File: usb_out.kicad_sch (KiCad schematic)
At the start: 30 parts, among them J6 USB_C_Receptacle_USB2.0, Q22 2N7002, U12 SY8105, U13 LM75B, U14 INA219AxD

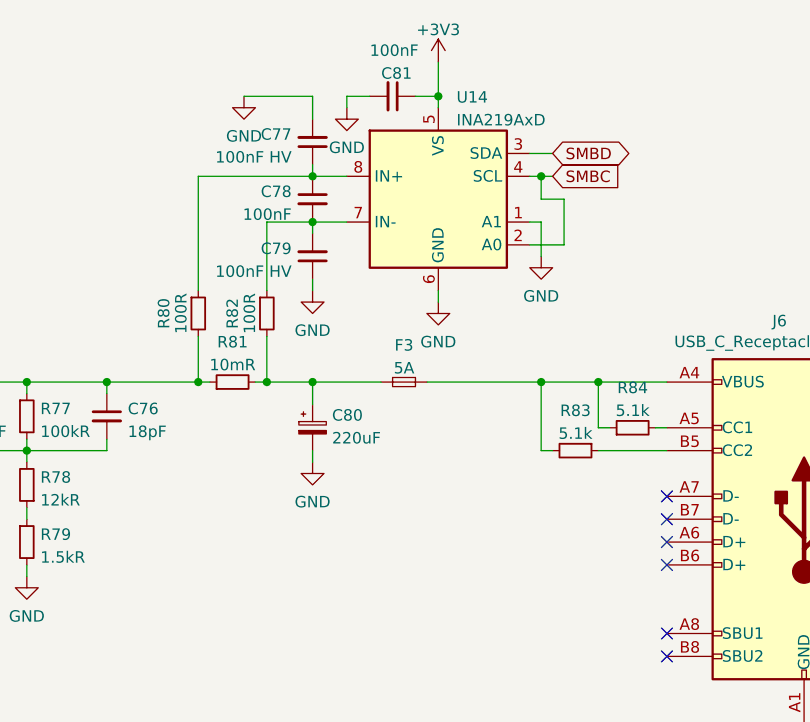
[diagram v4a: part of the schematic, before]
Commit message: Charger and step-down component placement
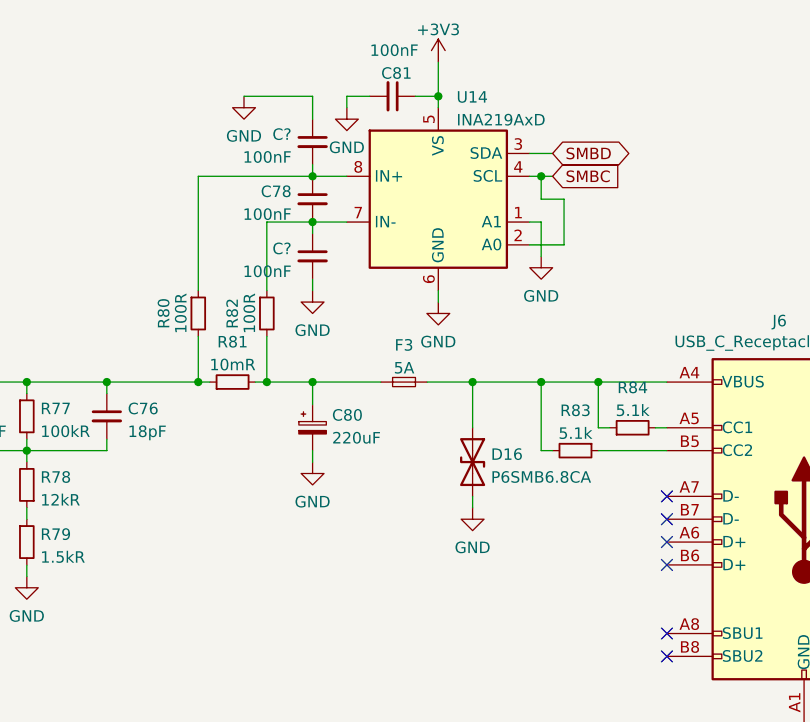
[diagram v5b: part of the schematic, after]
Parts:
- removed C77, C79: 100nF HV, Capacitor_SMD:C_0603_1608Metric, symbol Device:C_Small
- added C? (x2): 100nF, Capacitor_SMD:C_0402_1005Metric, symbol Device:C_Small
- added D16: P6SMB6.8CA, Diode_SMD:D_SMB, symbol Device:D_TVS
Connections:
- net GND: now also C?.1, C?.2, D16.2 (A2)
- net at F3.2, J6.A4 (VBUS), J6.A9 (VBUS)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: now also D16.1 (A1)
- net at C78.2, R82.1, U14.7 (IN-): now also C?.1
- net at C78.1, R80.1, U14.8 (IN+): now also C?.2
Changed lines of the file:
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@@
   (junction (at 142.24 66.04) (diameter 0) (color 0 0 0 0)
+  )
+  (junction (at 165.1 66.04) (diameter 0) (color 0 0 0 0)
   )
   (junction (at 179.07 66.04) (diameter 0) (color 0 0 0 0)
@@
     (stroke (width 0) (type default) (color 0 0 0 0))
   )
+  (wire (pts (xy 165.1 66.04) (xy 165.1 71.12))
+    (stroke (width 0) (type default) (color 0 0 0 0))
+  )
   (wire (pts (xy 81.28 129.54) (xy 82.55 129.54))
     (stroke (width 0) (type default) (color 0 0 0 0))
@@
     (stroke (width 0) (type default) (color 0 0 0 0))
   )
-  (wire (pts (xy 160.02 66.04) (xy 172.72 66.04))
+  (wire (pts (xy 160.02 66.04) (xy 165.1 66.04))
     (stroke (width 0) (type default) (color 0 0 0 0))
   )
@@
     (stroke (width 0) (type default) (color 0 0 0 0))
   )
+  (wire (pts (xy 165.1 78.74) (xy 165.1 80.01))
+    (stroke (width 0) (type default) (color 0 0 0 0))
+  )
   (wire (pts (xy 82.55 115.57) (xy 82.55 116.84))
     (stroke (width 0) (type default) (color 0 0 0 0))
@@
   )
   (wire (pts (xy 105.41 125.73) (xy 105.41 129.54))
+    (stroke (width 0) (type default) (color 0 0 0 0))
+  )
+  (wire (pts (xy 165.1 66.04) (xy 172.72 66.04))
     (stroke (width 0) (type default) (color 0 0 0 0))
   )
@@
     (pin "1")
   )
-  (symbol (lib_id "Device:C_Small") (at 147.32 52.07 0) (mirror x) (unit 1)
-    (in_bom yes) (on_board yes) (fields_autoplaced)
-    (property "Reference" "C79" (id 0) (at 144.996 51.2289 0)
-      (effects (font (size 1.27 1.27)) (justify right))
-    )
-    (property "Value" "100nF HV" (id 1) (at 144.996 53.7658 0)
-      (effects (font (size 1.27 1.27)) (justify right))
-    )
-    (property "Footprint" "Capacitor_SMD:C_0603_1608Metric" (id 2) (at 147.32 52.07 0)
-      (effects (font (size 1.27 1.27)) hide)
-    )
-    (property "Datasheet" "~" (id 3) (at 147.32 52.07 0)
-      (effects (font (size 1.27 1.27)) hide)
-    )
-    (property "LCSC" "C14663" (id 4) (at 147.32 52.07 90)
-      (effects (font (size 1.27 1.27)) hide)
-    )
-    (pin "1")
-    (pin "2")
-  )
   (symbol (lib_id "Regulator_Switching_Silergy:SY8105") (at 78.74 68.58 0) (unit 1)
     (in_bom yes) (on_board yes) (fields_autoplaced)
@@
     )
     (pin "1")
+  )
+  (symbol (lib_id "Device:D_TVS") (at 165.1 74.93 270) (unit 1)
+    (in_bom yes) (on_board yes) (fields_autoplaced)
+    (property "Reference" "D16" (id 0) (at 167.132 74.0953 90)
+      (effects (font (size 1.27 1.27)) (justify left))
+    )
+    (property "Value" "P6SMB6.8CA" (id 1) (at 167.132 76.6322 90)
+      (effects (font (size 1.27 1.27)) (justify left))
+    )
+    (property "Footprint" "Diode_SMD:D_SMB" (id 2) (at 165.1 74.93 0)
+      (effects (font (size 1.27 1.27)) hide)
+    )
+    (property "Datasheet" "~" (id 3) (at 165.1 74.93 0)
+      (effects (font (size 1.27 1.27)) hide)
+    )
+    (property "LCSC" "C78395" (id 4) (at 165.1 74.93 90)
+      (effects (font (size 1.27 1.27)) hide)
+    )
+    (pin "1")
+    (pin "2")
   )
   (symbol (lib_id "power:GND") (at 92.71 143.51 0) (unit 1)
@@
     )
     (pin "1")
-  )
-  (symbol (lib_id "Device:C_Small") (at 147.32 39.37 0) (mirror x) (unit 1)
-    (in_bom yes) (on_board yes) (fields_autoplaced)
-    (property "Reference" "C77" (id 0) (at 144.996 38.5289 0)
-      (effects (font (size 1.27 1.27)) (justify right))
-    )
-    (property "Value" "100nF HV" (id 1) (at 144.996 41.0658 0)
-      (effects (font (size 1.27 1.27)) (justify right))
-    )
-    (property "Footprint" "Capacitor_SMD:C_0603_1608Metric" (id 2) (at 147.32 39.37 0)
-      (effects (font (size 1.27 1.27)) hide)
-    )
-    (property "Datasheet" "~" (id 3) (at 147.32 39.37 0)
-      (effects (font (size 1.27 1.27)) hide)
-    )
-    (property "LCSC" "C14663" (id 4) (at 147.32 39.37 90)
-      (effects (font (size 1.27 1.27)) hide)
-    )
-    (pin "1")
-    (pin "2")
   )
   (symbol (lib_id "power:GND") (at 139.7 34.29 0) (unit 1)
@@
     (pin "8")
   )
+  (symbol (lib_id "Device:C_Small") (at 147.32 39.37 0) (mirror y) (unit 1)
+    (in_bom yes) (on_board yes)
+    (property "Reference" "C?" (id 0) (at 144.9959 38.5416 0)
+      (effects (font (size 1.27 1.27)) (justify left))
+    )
+    (property "Value" "100nF" (id 1) (at 144.9959 41.0785 0)
+      (effects (font (size 1.27 1.27)) (justify left))
+    )
+    (property "Footprint" "Capacitor_SMD:C_0402_1005Metric" (id 2) (at 147.32 39.37 0)
+      (effects (font (size 1.27 1.27)) hide)
+    )
+    (property "Datasheet" "~" (id 3) (at 147.32 39.37 0)
+      (effects (font (size 1.27 1.27)) hide)
+    )
+    (property "LCSC" "C1525" (id 4) (at 147.32 39.37 0)
+      (effects (font (size 1.27 1.27)) hide)
+    )
+    (pin "1")
+    (pin "2")
+  )
   (symbol (lib_id "Device:C_Small") (at 106.68 69.85 0) (unit 1)
     (in_bom yes) (on_board yes) (fields_autoplaced)
@@
     )
     (property "LCSC" "C270927" (id 4) (at 138.43 66.04 90)
+      (effects (font (size 1.27 1.27)) hide)
+    )
+    (pin "1")
+    (pin "2")
+  )
+  (symbol (lib_id "Device:C_Small") (at 147.32 52.07 0) (mirror y) (unit 1)
+    (in_bom yes) (on_board yes)
+    (property "Reference" "C?" (id 0) (at 144.9959 51.2416 0)
+      (effects (font (size 1.27 1.27)) (justify left))
+    )
+    (property "Value" "100nF" (id 1) (at 144.9959 53.7785 0)
+      (effects (font (size 1.27 1.27)) (justify left))
+    )
+    (property "Footprint" "Capacitor_SMD:C_0402_1005Metric" (id 2) (at 147.32 52.07 0)
+      (effects (font (size 1.27 1.27)) hide)
+    )
+    (property "Datasheet" "~" (id 3) (at 147.32 52.07 0)
+      (effects (font (size 1.27 1.27)) hide)
+    )
+    (property "LCSC" "C1525" (id 4) (at 147.32 52.07 0)
       (effects (font (size 1.27 1.27)) hide)
     )
@@
     (pin "2")
   )
+  (symbol (lib_id "power:GND") (at 165.1 80.01 0) (unit 1)
+    (in_bom yes) (on_board yes) (fields_autoplaced)
+    (property "Reference" "#PWR0260" (id 0) (at 165.1 86.36 0)
+      (effects (font (size 1.27 1.27)) hide)
+    )
+    (property "Value" "GND" (id 1) (at 165.1 84.4534 0))
+    (property "Footprint" "" (id 2) (at 165.1 80.01 0)
+      (effects (font (size 1.27 1.27)) hide)
+    )
+    (property "Datasheet" "" (id 3) (at 165.1 80.01 0)
+      (effects (font (size 1.27 1.27)) hide)
+    )
+    (pin "1")
+  )
   (symbol (lib_id "power:+3V3") (at 161.29 30.48 0) (unit 1)

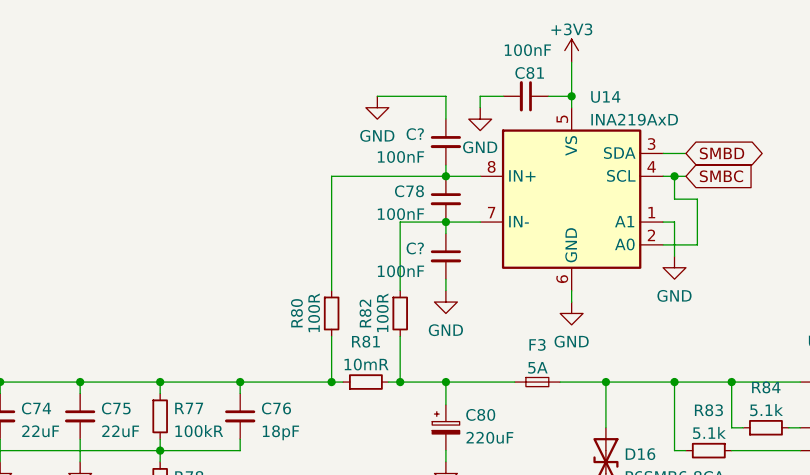
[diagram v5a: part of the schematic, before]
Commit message: Partial DC out step-up component placement
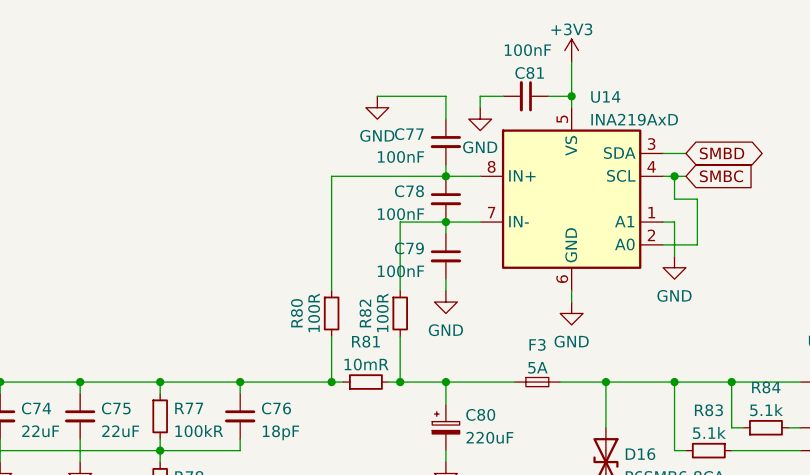
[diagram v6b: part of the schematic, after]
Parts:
- gave numbers to parts that had none: 2
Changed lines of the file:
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@@
   (symbol (lib_id "Device:C_Small") (at 147.32 39.37 0) (mirror y) (unit 1)
     (in_bom yes) (on_board yes)
-    (property "Reference" "C?" (id 0) (at 144.9959 38.5416 0)
+    (property "Reference" "C77" (id 0) (at 144.9959 38.5416 0)
       (effects (font (size 1.27 1.27)) (justify left))
     )
@@
   (symbol (lib_id "Device:C_Small") (at 147.32 52.07 0) (mirror y) (unit 1)
     (in_bom yes) (on_board yes)
-    (property "Reference" "C?" (id 0) (at 144.9959 51.2416 0)
+    (property "Reference" "C79" (id 0) (at 144.9959 51.2416 0)
       (effects (font (size 1.27 1.27)) (justify left))
     )

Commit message: Partial layout
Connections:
- net VBUS: now reaches D16.1 (A1), F3.2, J6.A4 (VBUS), J6.A9 (VBUS), J6.B4 (VBUS), J6.B9 (VBUS), R83.2, R84.1
- net VOUT: now reaches C74.1, C75.1, C76.1, L4.2, R77.1, R80.2, R81.1
- net LX: now reaches C72.1, L4.1, U12.5 (LX)
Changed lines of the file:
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@@
     (stroke (width 0) (type default) (color 0 0 0 0))
+  )
+  (label "VOUT" (at 115.57 66.04 0)
+    (effects (font (size 1.27 1.27)) (justify left bottom))
+  )
+  (label "LX" (at 88.9 58.42 270)
+    (effects (font (size 1.27 1.27)) (justify right bottom))
+  )
+  (label "VBUS" (at 172.72 66.04 0)
+    (effects (font (size 1.27 1.27)) (justify left bottom))
   )
   (global_label "USB_OUT_OFF" (shape input) (at 53.34 85.09 180) (fields_autoplaced)
@@
       (effects (font (size 1.27 1.27)) hide)
     )
-    (property "Datasheet" "https://www.usb.org/sites/default/files/documents/usb_type-c.zip" (id 3) (at 198.12 81.28 0)
-      (effects (font (size 1.27 1.27)) hide)
-    )
+    (property "Datasheet" "https://datasheet.lcsc.com/lcsc/2103051833_Jing-Extension-of-the-Electronic-Co.-918-418K2023S40001_C167321.pdf" (id 3) (at 198.12 81.28 0)
+      (effects (font (size 1.27 1.27)) hide)
+    )
